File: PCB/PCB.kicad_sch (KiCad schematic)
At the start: 17 parts, among them J1 Conn_01x06_Female, J2 5054332681, U13 74HC165, U15 LT3042xMSE, U16 74HC165

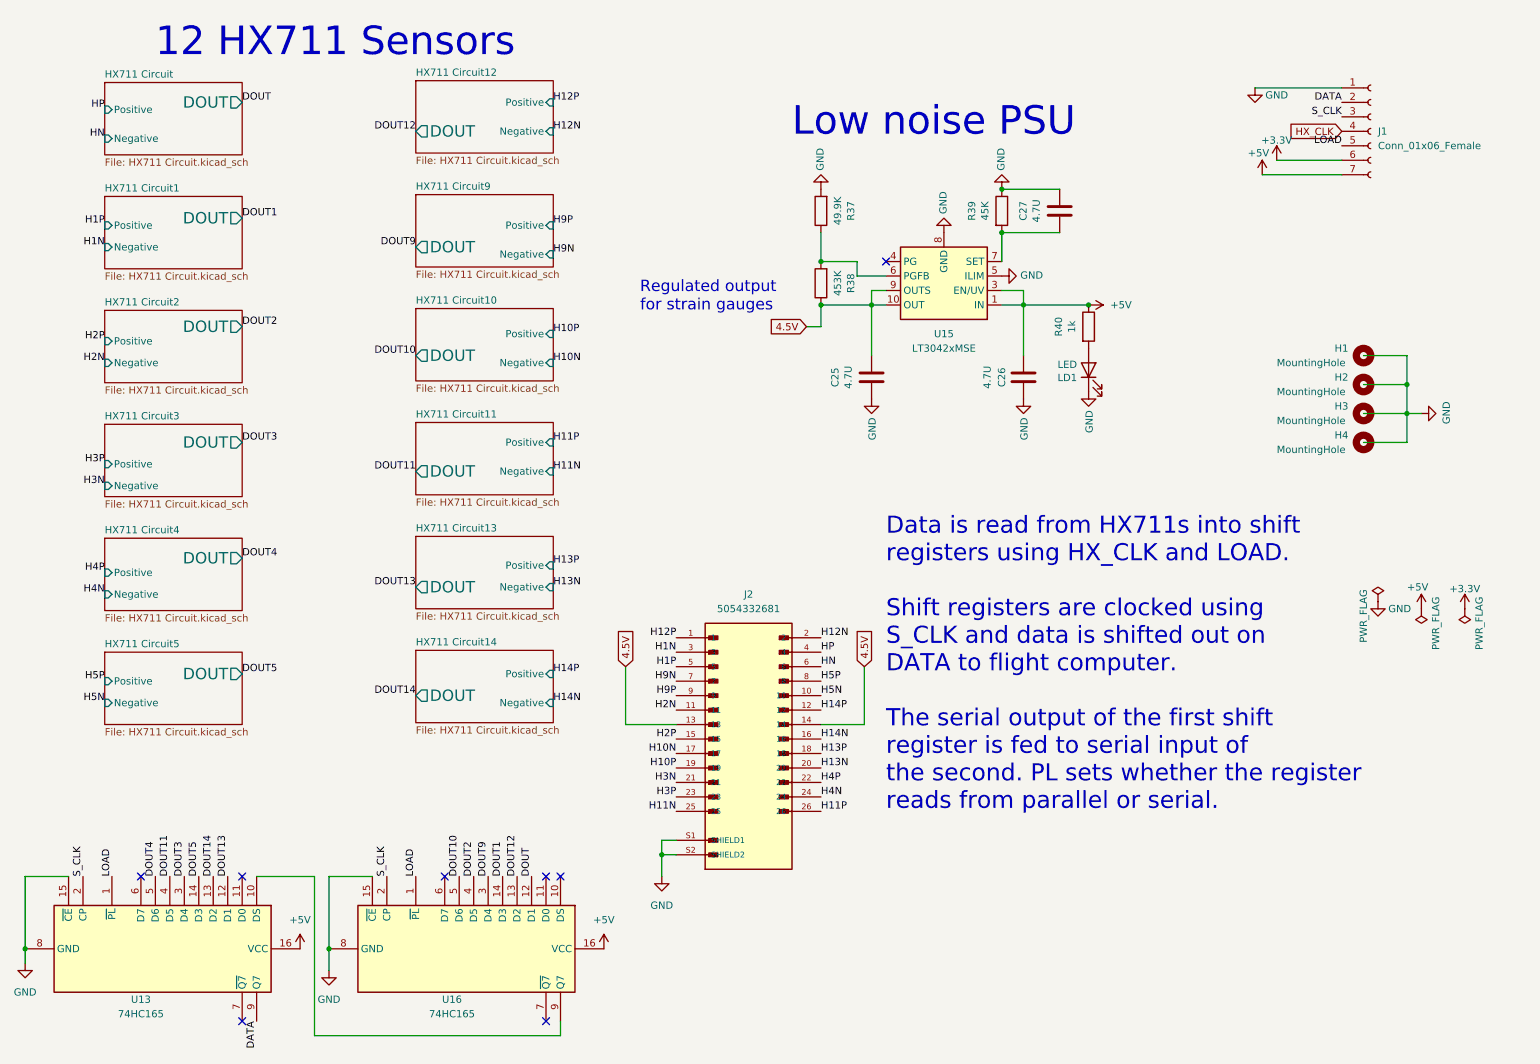
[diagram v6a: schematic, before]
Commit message: Added test points and changed labels
Added test points for nearly every single cable. Labels on individual sections changed to better reflect the actual board.
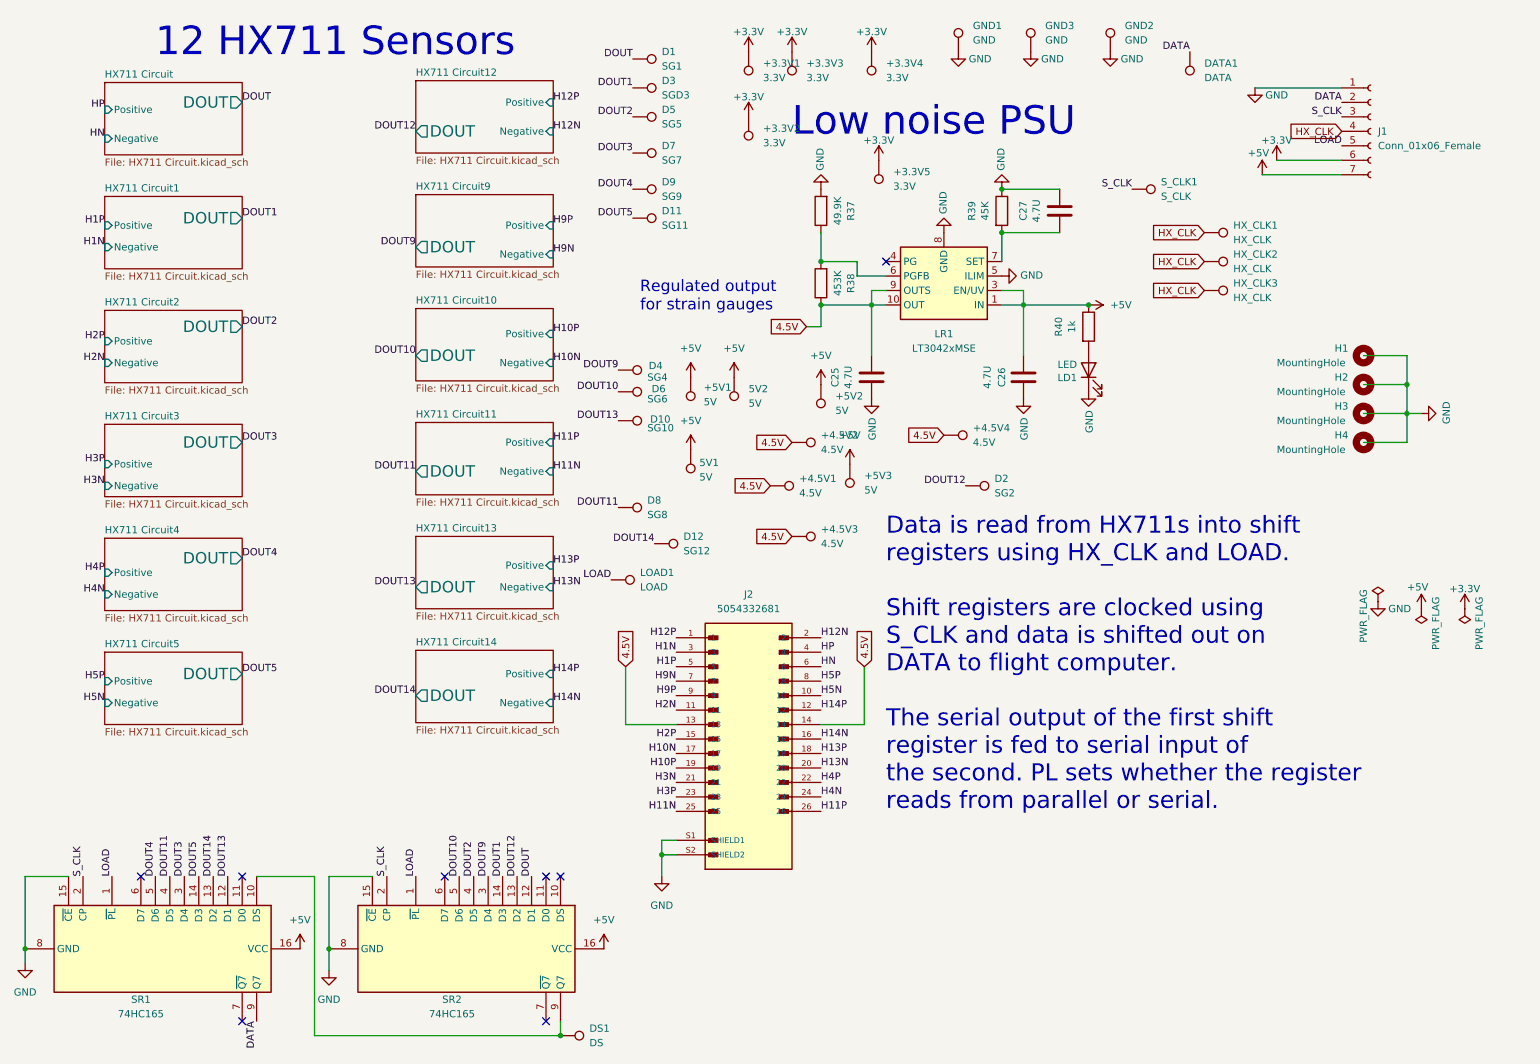
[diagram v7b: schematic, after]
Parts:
- added +3.3V1, +3.3V2, +3.3V3, +3.3V4, +3.3V5: 3.3V, TestPoint:TestPoint_THTPad_1.0x1.0mm_Drill0.5mm, symbol Connector:TestPoint
- added +4.5V1, +4.5V2, +4.5V3, +4.5V4: 4.5V, TestPoint:TestPoint_THTPad_1.0x1.0mm_Drill0.5mm, symbol Connector:TestPoint
- added +5V1, +5V2, +5V3, 5V1, 5V2: 5V, TestPoint:TestPoint_THTPad_1.0x1.0mm_Drill0.5mm, symbol Connector:TestPoint
- added D1: SG1, TestPoint:TestPoint_THTPad_1.0x1.0mm_Drill0.5mm, symbol Connector:TestPoint
- added D10: SG10, TestPoint:TestPoint_THTPad_1.0x1.0mm_Drill0.5mm, symbol Connector:TestPoint
- added D11: SG11, TestPoint:TestPoint_THTPad_1.0x1.0mm_Drill0.5mm, symbol Connector:TestPoint
- added D12: SG12, TestPoint:TestPoint_THTPad_1.0x1.0mm_Drill0.5mm, symbol Connector:TestPoint
- added D2: SG2, TestPoint:TestPoint_THTPad_1.0x1.0mm_Drill0.5mm, symbol Connector:TestPoint
- added D3: SGD3, TestPoint:TestPoint_THTPad_1.0x1.0mm_Drill0.5mm, symbol Connector:TestPoint
- added D4: SG4, TestPoint:TestPoint_THTPad_1.0x1.0mm_Drill0.5mm, symbol Connector:TestPoint
- added D5: SG5, TestPoint:TestPoint_THTPad_1.0x1.0mm_Drill0.5mm, symbol Connector:TestPoint
- added D6: SG6, TestPoint:TestPoint_THTPad_1.0x1.0mm_Drill0.5mm, symbol Connector:TestPoint
- added D7: SG7, TestPoint:TestPoint_THTPad_1.0x1.0mm_Drill0.5mm, symbol Connector:TestPoint
- added D8: SG8, TestPoint:TestPoint_THTPad_1.0x1.0mm_Drill0.5mm, symbol Connector:TestPoint
- added D9: SG9, TestPoint:TestPoint_THTPad_1.0x1.0mm_Drill0.5mm, symbol Connector:TestPoint
- added DATA1: DATA, TestPoint:TestPoint_THTPad_1.0x1.0mm_Drill0.5mm, symbol Connector:TestPoint
- added DS1: DS, TestPoint:TestPoint_THTPad_1.0x1.0mm_Drill0.5mm, symbol Connector:TestPoint
- added GND1, GND2, GND3: GND, TestPoint:TestPoint_THTPad_1.0x1.0mm_Drill0.5mm, symbol Connector:TestPoint
- added HX_CLK1, HX_CLK2, HX_CLK3: HX_CLK, TestPoint:TestPoint_THTPad_1.0x1.0mm_Drill0.5mm, symbol Connector:TestPoint
- added LOAD1: LOAD, TestPoint:TestPoint_THTPad_1.0x1.0mm_Drill0.5mm, symbol Connector:TestPoint
- added S_CLK1: S_CLK, TestPoint:TestPoint_THTPad_1.0x1.0mm_Drill0.5mm, symbol Connector:TestPoint
- renumbered U15 to LR1, U13 to SR1, U16 to SR2
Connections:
- net +3.3V: now also +3.3V1.1, +3.3V2.1, +3.3V3.1, +3.3V4.1, +3.3V5.1
- net +5V: now also +5V1.1, +5V2.1, +5V3.1, 5V1.1, 5V2.1
- net 4.5V: now also +4.5V1.1, +4.5V2.1, +4.5V3.1, +4.5V4.1
- net DATA: now also DATA1.1
- net DOUT: now also D1.1
- net DOUT1: now also D3.1
- net DOUT10: now also D6.1
- net DOUT11: now also D8.1
- net DOUT12: now also D2.1
- net DOUT13: now also D10.1
- net DOUT14: now also D12.1
- net DOUT2: now also D5.1
- net DOUT3: now also D7.1
- net DOUT4: now also D9.1
- net DOUT5: now also D11.1
- net DOUT9: now also D4.1
- net GND: now also GND1.1, GND2.1, GND3.1
- net HX_CLK: now also HX_CLK1.1, HX_CLK2.1, HX_CLK3.1
- net LOAD: now also LOAD1.1
- net S_CLK: now also S_CLK1.1
- net at SR1.10 (DS), SR2.9 (Q7): now also DS1.1

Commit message: Silkscreen updated
The strain gauges are correctly labeled now as well as the test points for all individual hx711 amplifiers. All the voltages are completely labeled as well. There are many 4.5V, 5V and 3.3V  test points. Every digital signal has its test point. To place the test points, I replaced some of the vias with test points or spliced two lines together.
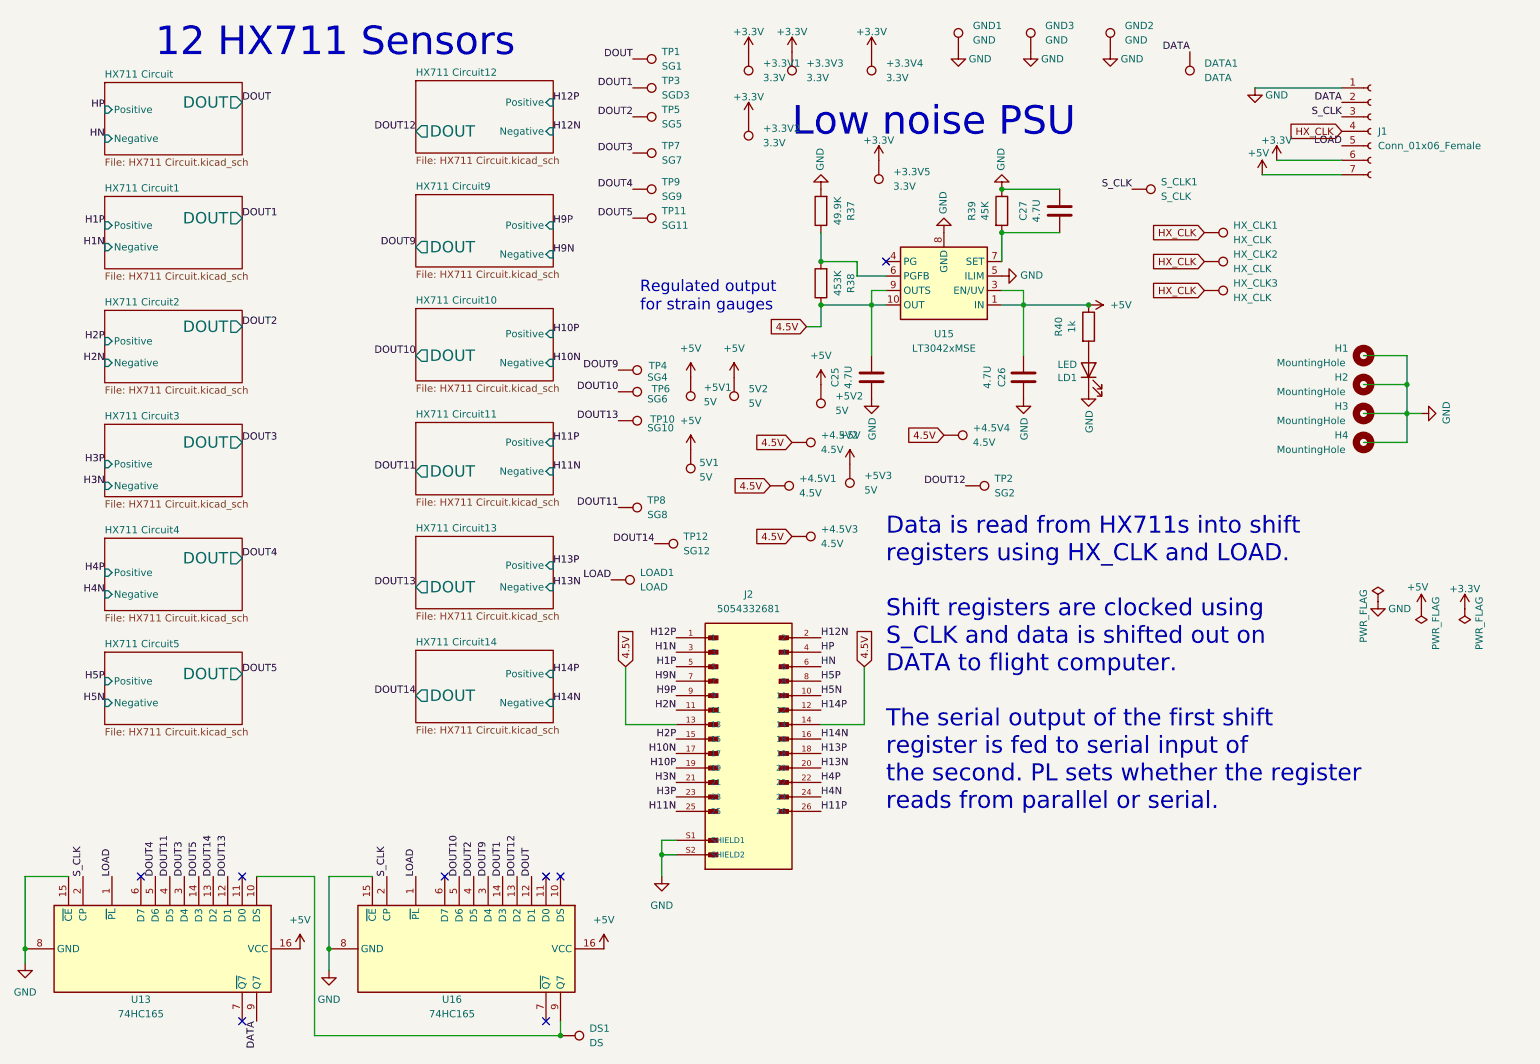
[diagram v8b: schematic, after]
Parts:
- renumbered D1 to TP1, D10 to TP10, D11 to TP11, D12 to TP12, D2 to TP2, D3 to TP3, D4 to TP4, D5 to TP5, D6 to TP6, D7 to TP7, D8 to TP8, D9 to TP9, SR1 to U13, LR1 to U15, SR2 to U16
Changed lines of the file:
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@@
 		(dnp no)
 		(fields_autoplaced yes)
-		(property "Reference" "D3"
+		(property "Reference" "TP3"
 			(at 132.08 25.3999 90)
 			(effects
@@
 			(project "PCB"
 				(path "/b6270a28-e0d9-4655-a18a-03dbf007b940"
-					(reference "D3")
+					(reference "TP3")
 					(unit 1)
 				)
@@
 		(dnp no)
 		(fields_autoplaced yes)
-		(property "Reference" "D2"
+		(property "Reference" "TP2"
 			(at 190.5 95.2499 90)
 			(effects
@@
 			(project "PCB"
 				(path "/b6270a28-e0d9-4655-a18a-03dbf007b940"
-					(reference "D2")
+					(reference "TP2")
 					(unit 1)
 				)
@@
 		(on_board yes)
 		(dnp no)
-		(property "Reference" "SR1"
+		(property "Reference" "U13"
 			(at 40.64 186.69 90)
 			(effects
@@
 			(project "PCB"
 				(path "/b6270a28-e0d9-4655-a18a-03dbf007b940"
-					(reference "SR1")
+					(reference "U13")
 					(unit 1)
 				)
@@
 		(dnp no)
 		(fields_autoplaced yes)
-		(property "Reference" "LR1"
+		(property "Reference" "U15"
 			(at 181.61 69.85 0)
 			(effects
@@
 			(project "PCB"
 				(path "/b6270a28-e0d9-4655-a18a-03dbf007b940"
-					(reference "LR1")
+					(reference "U15")
 					(unit 1)
 				)
@@
 		(dnp no)
 		(fields_autoplaced yes)
-		(property "Reference" "D8"
+		(property "Reference" "TP8"
 			(at 129.54 99.0599 90)
 			(effects
@@
 			(project "PCB"
 				(path "/b6270a28-e0d9-4655-a18a-03dbf007b940"
-					(reference "D8")
+					(reference "TP8")
 					(unit 1)
 				)
@@
 		(dnp no)
 		(fields_autoplaced yes)
-		(property "Reference" "D7"
+		(property "Reference" "TP7"
 			(at 132.08 36.8299 90)
 			(effects
@@
 			(project "PCB"
 				(path "/b6270a28-e0d9-4655-a18a-03dbf007b940"
-					(reference "D7")
+					(reference "TP7")
 					(unit 1)
 				)
@@
 		(dnp no)
 		(fields_autoplaced yes)
-		(property "Reference" "D12"
+		(property "Reference" "TP12"
 			(at 135.89 105.4099 90)
 			(effects
@@
 			(project "PCB"
 				(path "/b6270a28-e0d9-4655-a18a-03dbf007b940"
-					(reference "D12")
+					(reference "TP12")
 					(unit 1)
 				)
@@
 		(on_board yes)
 		(dnp no)
-		(property "Reference" "D6"
+		(property "Reference" "TP6"
 			(at 130.302 79.502 90)
 			(effects
@@
 			(project "PCB"
 				(path "/b6270a28-e0d9-4655-a18a-03dbf007b940"
-					(reference "D6")
+					(reference "TP6")
 					(unit 1)
 				)
@@
 		(on_board yes)
 		(dnp no)
-		(property "Reference" "D4"
+		(property "Reference" "TP4"
 			(at 129.794 75.438 90)
 			(effects
@@
 			(project "PCB"
 				(path "/b6270a28-e0d9-4655-a18a-03dbf007b940"
-					(reference "D4")
+					(reference "TP4")
 					(unit 1)
 				)
@@
 		(on_board yes)
 		(dnp no)
-		(property "Reference" "D10"
+		(property "Reference" "TP10"
 			(at 130.048 84.836 90)
 			(effects
@@
 			(project "PCB"
 				(path "/b6270a28-e0d9-4655-a18a-03dbf007b940"
-					(reference "D10")
+					(reference "TP10")
 					(unit 1)
 				)
@@
 		(dnp no)
 		(fields_autoplaced yes)
-		(property "Reference" "D1"
+		(property "Reference" "TP1"
 			(at 132.08 20.3199 90)
 			(effects
@@
 			(project "PCB"
 				(path "/b6270a28-e0d9-4655-a18a-03dbf007b940"
-					(reference "D1")
+					(reference "TP1")
 					(unit 1)
 				)
@@
 		(on_board yes)
 		(dnp no)
-		(property "Reference" "SR2"
+		(property "Reference" "U16"
 			(at 95.25 186.69 90)
 			(effects
@@
 			(project "PCB"
 				(path "/b6270a28-e0d9-4655-a18a-03dbf007b940"
-					(reference "SR2")
+					(reference "U16")
 					(unit 1)
 				)
@@
 		(dnp no)
 		(fields_autoplaced yes)
-		(property "Reference" "D11"
+		(property "Reference" "TP11"
 			(at 132.08 48.2599 90)
 			(effects
@@
 			(project "PCB"
 				(path "/b6270a28-e0d9-4655-a18a-03dbf007b940"
-					(reference "D11")
+					(reference "TP11")
 					(unit 1)
 				)
@@
 		(dnp no)
 		(fields_autoplaced yes)
-		(property "Reference" "D5"
+		(property "Reference" "TP5"
 			(at 132.08 30.4799 90)
 			(effects
@@
 			(project "PCB"
 				(path "/b6270a28-e0d9-4655-a18a-03dbf007b940"
-					(reference "D5")
+					(reference "TP5")
 					(unit 1)
 				)
@@
 		(dnp no)
 		(fields_autoplaced yes)
-		(property "Reference" "D9"
+		(property "Reference" "TP9"
 			(at 132.08 43.1799 90)
 			(effects
@@
 			(project "PCB"
 				(path "/b6270a28-e0d9-4655-a18a-03dbf007b940"
-					(reference "D9")
+					(reference "TP9")
 					(unit 1)
 				)
